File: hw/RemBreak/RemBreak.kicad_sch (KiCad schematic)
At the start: 7 parts, among them J1 Conn_01x03, J2 Conn_01x04

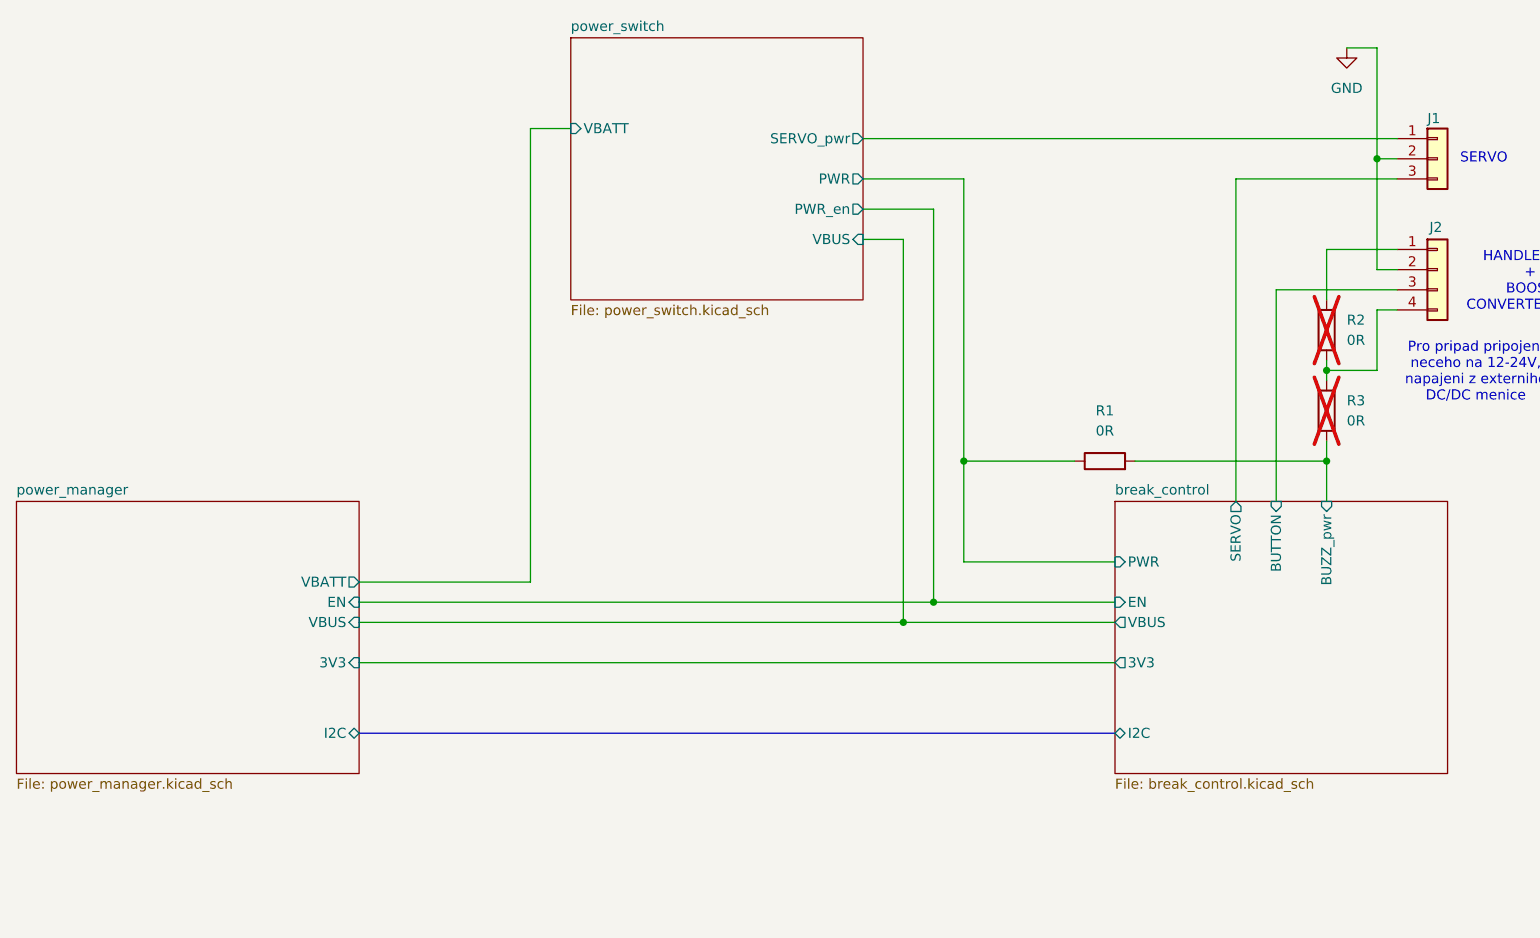
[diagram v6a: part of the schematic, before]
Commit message: changes in power line sharing in progress
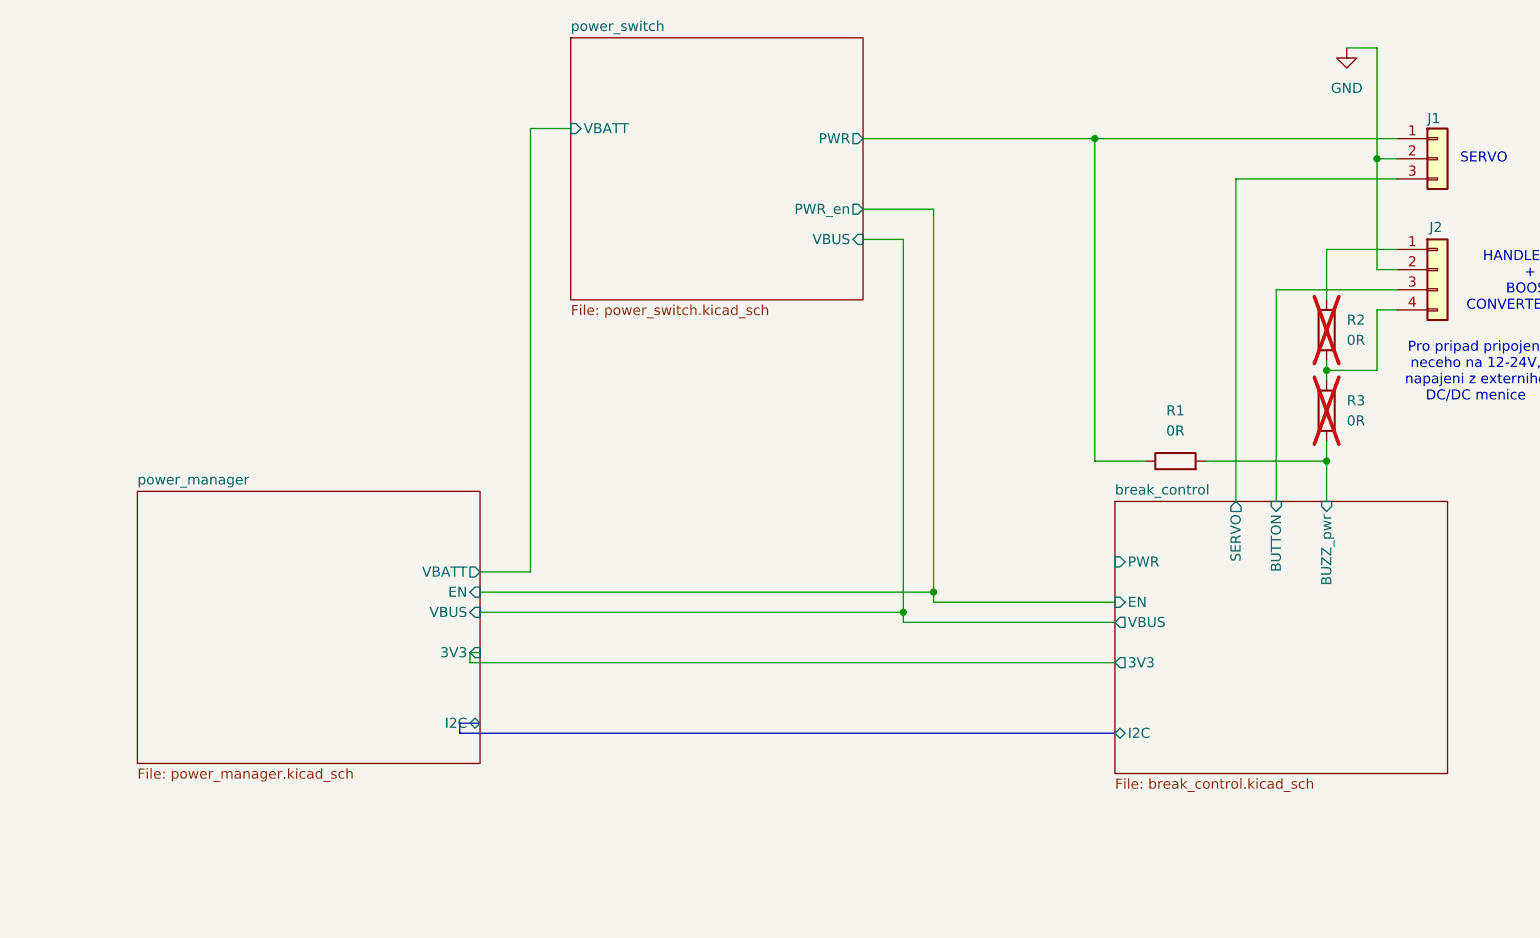
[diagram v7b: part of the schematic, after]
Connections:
- net break_control/PWR: no longer R1.1
- net power_switch/SERVO_pwr renamed power_switch/PWR
- net power_switch/PWR: now also R1.1
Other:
- sheet power_switch ports: added none; removed SERVO_pwr
- moved on the sheet: R1
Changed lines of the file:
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@@
-	)
-	(junction
-		(at 154.94 116.84)
-		(diameter 0)
-		(color 0 0 0 0)
 	)
 	(junction
@@
 	)
 	(junction
-		(at 158.75 99.06)
+		(at 175.26 58.42)
 		(diameter 0)
 		(color 0 0 0 0)
 	)
 	(junction
-		(at 151.13 119.38)
+		(at 154.94 115.57)
 		(diameter 0)
 		(color 0 0 0 0)
 	)
+	(junction
+		(at 151.13 118.11)
+		(diameter 0)
+		(color 0 0 0 0)
+	)
 	(wire
 		(pts
@@
 	(wire
 		(pts
-			(xy 158.75 111.76) (xy 158.75 99.06)
-		)
-		(stroke
-			(width 0)
-			(type default)
-		)
-	)
-	(wire
-		(pts
 			(xy 151.13 119.38) (xy 177.8 119.38)
 		)
@@
 	(wire
 		(pts
-			(xy 82.55 114.3) (xy 104.14 114.3)
+			(xy 97.79 113.03) (xy 104.14 113.03)
 		)
 		(stroke
@@
 	(bus
 		(pts
-			(xy 82.55 133.35) (xy 177.8 133.35)
+			(xy 97.79 132.08) (xy 95.25 132.08)
 		)
 		(stroke
@@
 	(wire
 		(pts
-			(xy 158.75 63.5) (xy 158.75 99.06)
-		)
-		(stroke
-			(width 0)
-			(type default)
-		)
-	)
-	(wire
-		(pts
 			(xy 154.94 116.84) (xy 177.8 116.84)
 		)
@@
 	(wire
 		(pts
+			(xy 175.26 99.06) (xy 181.61 99.06)
+		)
+		(stroke
+			(width 0)
+			(type default)
+		)
+	)
+	(wire
+		(pts
 			(xy 198.12 77.47) (xy 213.36 77.47)
 		)
@@
 	(wire
 		(pts
-			(xy 146.05 58.42) (xy 213.36 58.42)
-		)
-		(stroke
-			(width 0)
-			(type default)
-		)
-	)
-	(wire
-		(pts
 			(xy 146.05 67.31) (xy 154.94 67.31)
 		)
@@
 	(wire
 		(pts
+			(xy 175.26 58.42) (xy 213.36 58.42)
+		)
+		(stroke
+			(width 0)
+			(type default)
+		)
+	)
+	(wire
+		(pts
+			(xy 96.52 124.46) (xy 177.8 124.46)
+		)
+		(stroke
+			(width 0)
+			(type default)
+		)
+	)
+	(wire
+		(pts
 			(xy 210.82 46.99) (xy 207.01 46.99)
 		)
@@
 	(wire
 		(pts
+			(xy 154.94 115.57) (xy 154.94 116.84)
+		)
+		(stroke
+			(width 0)
+			(type default)
+		)
+	)
+	(bus
+		(pts
+			(xy 95.25 132.08) (xy 95.25 133.35)
+		)
+		(stroke
+			(width 0)
+			(type default)
+		)
+	)
+	(wire
+		(pts
 			(xy 204.47 99.06) (xy 204.47 96.52)
 		)
@@
 	(wire
 		(pts
-			(xy 82.55 119.38) (xy 151.13 119.38)
+			(xy 97.79 118.11) (xy 151.13 118.11)
 		)
 		(stroke
@@
 	(wire
 		(pts
-			(xy 146.05 63.5) (xy 158.75 63.5)
+			(xy 146.05 58.42) (xy 175.26 58.42)
 		)
 		(stroke
@@
 	(wire
 		(pts
-			(xy 158.75 99.06) (xy 172.72 99.06)
+			(xy 175.26 58.42) (xy 175.26 99.06)
 		)
 		(stroke
@@
 	(wire
 		(pts
-			(xy 151.13 71.12) (xy 151.13 119.38)
-		)
-		(stroke
-			(width 0)
-			(type default)
-		)
-	)
-	(wire
-		(pts
-			(xy 104.14 57.15) (xy 104.14 114.3)
-		)
-		(stroke
-			(width 0)
-			(type default)
-		)
-	)
-	(wire
-		(pts
-			(xy 177.8 111.76) (xy 158.75 111.76)
+			(xy 151.13 71.12) (xy 151.13 118.11)
+		)
+		(stroke
+			(width 0)
+			(type default)
+		)
+	)
+	(wire
+		(pts
+			(xy 104.14 57.15) (xy 104.14 113.03)
 		)
 		(stroke
@@
 	(wire
 		(pts
-			(xy 82.55 124.46) (xy 177.8 124.46)
+			(xy 97.79 123.19) (xy 96.52 123.19)
+		)
+		(stroke
+			(width 0)
+			(type default)
+		)
+	)
+	(bus
+		(pts
+			(xy 95.25 133.35) (xy 177.8 133.35)
 		)
 		(stroke
@@
 	(wire
 		(pts
-			(xy 180.34 99.06) (xy 204.47 99.06)
-		)
-		(stroke
-			(width 0)
-			(type default)
-		)
-	)
-	(wire
-		(pts
-			(xy 82.55 116.84) (xy 154.94 116.84)
-		)
-		(stroke
-			(width 0)
-			(type default)
-		)
-	)
-	(wire
-		(pts
-			(xy 154.94 67.31) (xy 154.94 116.84)
+			(xy 189.23 99.06) (xy 204.47 99.06)
+		)
+		(stroke
+			(width 0)
+			(type default)
+		)
+	)
+	(wire
+		(pts
+			(xy 97.79 115.57) (xy 154.94 115.57)
+		)
+		(stroke
+			(width 0)
+			(type default)
+		)
+	)
+	(wire
+		(pts
+			(xy 154.94 67.31) (xy 154.94 115.57)
 		)
 		(stroke
@@
 		(pts
 			(xy 109.22 57.15) (xy 104.14 57.15)
+		)
+		(stroke
+			(width 0)
+			(type default)
+		)
+	)
+	(wire
+		(pts
+			(xy 151.13 118.11) (xy 151.13 119.38)
+		)
+		(stroke
+			(width 0)
+			(type default)
+		)
+	)
+	(wire
+		(pts
+			(xy 96.52 123.19) (xy 96.52 124.46)
 		)
 		(stroke
@@
 	(symbol
 		(lib_id "Device:R")
-		(at 176.53 99.06 90)
+		(at 185.42 99.06 90)
 		(unit 1)
 		(exclude_from_sim no)
@@
 		(fields_autoplaced yes)
 		(property "Reference" "R1"
-			(at 176.53 92.71 90)
+			(at 185.42 92.71 90)
 			(effects
 				(font
@@
 		)
 		(property "Value" "0R"
-			(at 176.53 95.25 90)
+			(at 185.42 95.25 90)
 			(effects
 				(font
@@
 		)
 		(property "Footprint" "Resistor_SMD:R_0805_2012Metric"
-			(at 176.53 100.838 90)
+			(at 185.42 100.838 90)
 			(effects
 				(font
@@
 		)
 		(property "Datasheet" "~"
-			(at 176.53 99.06 0)
+			(at 185.42 99.06 0)
 			(effects
 				(font
@@
 		)
 		(property "Description" "Resistor"
-			(at 176.53 99.06 0)
+			(at 185.42 99.06 0)
 			(effects
 				(font
@@
 			)
 		)
-		(pin "SERVO_pwr" output
+		(pin "PWR" output
 			(at 146.05 58.42 0)
-			(effects
-				(font
-					(size 1.27 1.27)
-				)
-				(justify right)
-			)
-		)
-		(pin "PWR" output
-			(at 146.05 63.5 0)
 			(effects
 				(font
@@
 	)
 	(sheet
-		(at 39.37 104.14)
+		(at 54.61 102.87)
 		(size 43.18 34.29)
 		(exclude_from_sim no)
@@
 		)
 		(property "Sheetname" "power_manager"
-			(at 39.37 103.4284 0)
+			(at 54.61 102.1584 0)
 			(effects
 				(font
@@
 		)
 		(property "Sheetfile" "power_manager.kicad_sch"
-			(at 39.37 139.0146 0)
+			(at 54.61 137.7446 0)
 			(effects
 				(font
@@
 		)
 		(pin "I2C" bidirectional
-			(at 82.55 133.35 0)
+			(at 97.79 132.08 0)
 			(effects
 				(font
@@
 		)
 		(pin "3V3" input
-			(at 82.55 124.46 0)
+			(at 97.79 123.19 0)
 			(effects
 				(font
@@
 		)
 		(pin "VBATT" output
-			(at 82.55 114.3 0)
+			(at 97.79 113.03 0)
 			(effects
 				(font
@@
 		)
 		(pin "VBUS" input
-			(at 82.55 119.38 0)
+			(at 97.79 118.11 0)
 			(effects
 				(font
@@
 		)
 		(pin "EN" input
-			(at 82.55 116.84 0)
-			(effects
-				(font
+			(at 97.79 115.57 0)
+			(effects
+				(font

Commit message: schematics development in progress
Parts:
- removed J1: Conn_01x03, Connector_PinHeader_2.54mm:PinHeader_1x03_P2.54mm_Vertical_SMD_Pin1Left, symbol Connector_Generic:Conn_01x03
- removed J2: Conn_01x04, TerminalBlock_Phoenix:TerminalBlock_Phoenix_MPT-0,5-4-2.54_1x04_P2.54mm_Horizontal, symbol Connector_Generic:Conn_01x04
- added J2: Conn_02x06_Odd_Even, Connector_PinHeader_2.54mm:PinHeader_2x06_P2.54mm_Vertical_SMD, symbol Connector_Generic:Conn_02x06_Odd_Even
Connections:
- net power_switch/PWR: no longer R1.1
- net break_control/BUZZ_pwr: no longer names the net of R1.2
- net break_control/BUZZ_pwr: no longer R3.1
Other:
- sheet break_control ports: added none; removed 3V3, BUZZ_pwr, EN, SERVO
- sheet power_manager ports: added none; removed VBUS
- sheet power_switch ports: added EN; removed PWR_en
- note added: "Accelerometer I2C address: 0x68 + R/W"
- note added: "BATTERY INDICATOR"
- moved on the sheet: R1, R2, R3
